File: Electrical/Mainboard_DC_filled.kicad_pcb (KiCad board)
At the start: 2 copper layers, 108 x 88.9 mm, 73 parts, among them J1 Serial Connector, Q1 TIP41C, Q2 TIP41C, U1 L7805CV, U10 6N137, U11 6N137, U12 6N137, U13 6N137, U2 Teensy3.5, U3 L7805CV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

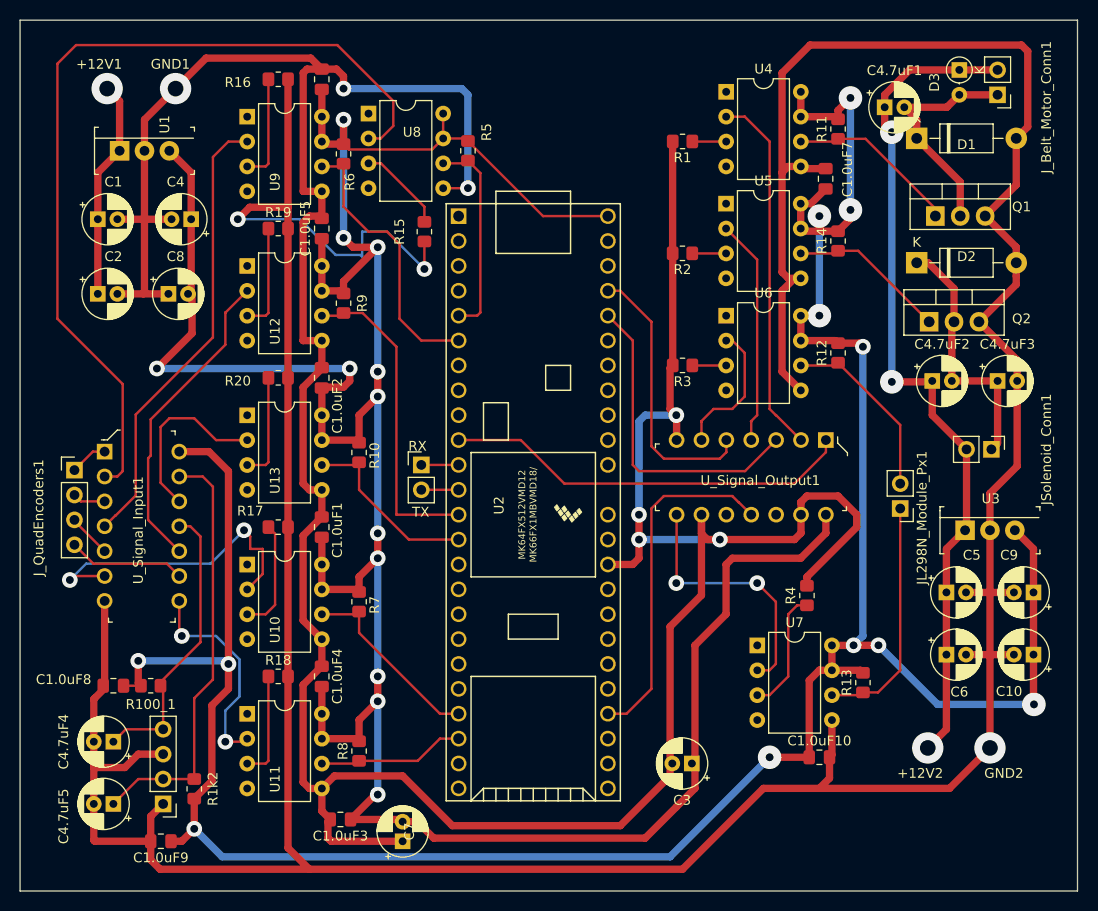
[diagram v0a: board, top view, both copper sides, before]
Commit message: Fixed PCB Error
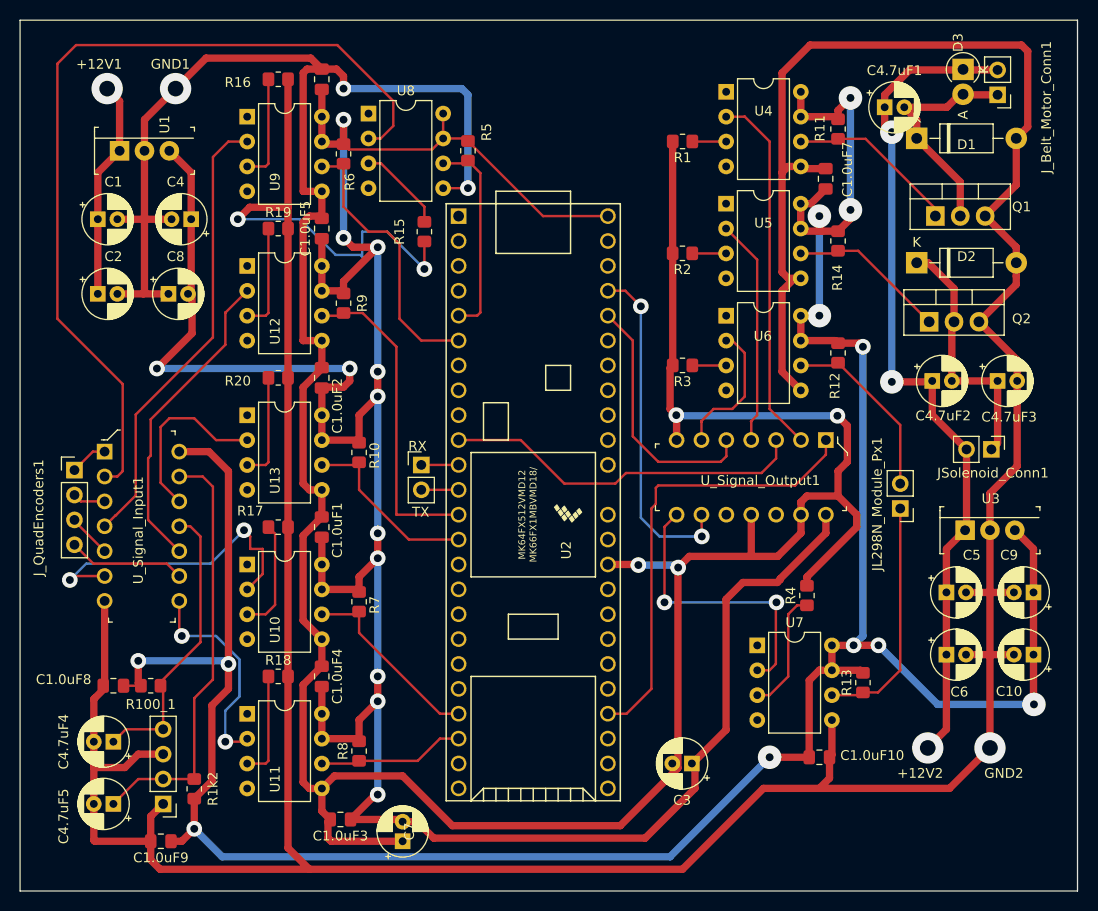
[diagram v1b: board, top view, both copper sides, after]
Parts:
- D3: footprint Diode_THT:D_DO-35_SOD27_P2.54mm_Vertical_AnodeUp -> Diode_THT:D_DO-41_SOD81_P2.54mm_Vertical_AnodeUp
- moved D3 0.39 mm to (196.0, 49.5)
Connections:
- U2 pad 39: unconnected-(U2-Pad39) -> GND1
- U8 pad 2: Net-(U8-Pad2) -> Net-(U8-A)
- U8 pad 3: Net-(R15-Pad1) -> Net-(U8-C)
- U8 pad 6: /QuadDecode1A_Px -> /pg2/QuadDecode1A_Px
- U_Signal_Output1 pad 1: /Print_Solenoid -> /Belt_Motor
- U_Signal_Output1 pad 11: /Belt_Motor -> GND1
- U_Signal_Output1 pad 3: /Px_Motor_Left -> /Print_Solenoid
- U_Signal_Output1 pad 5: /Px_Motor_Right -> /Px_Motor_Left
- U_Signal_Output1 pad 9: GND1 -> /Px_Motor_Right
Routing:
- net /Belt_Motor: track 35.4 -> 46.5 mm
- net /Px_Motor_Right: track 28.2 -> 35.1 mm, vias 0 -> 2
- net /Px_Motor_Left: track 32.5 -> 25.9 mm
- net /Print_Solenoid: track 41.9 -> 37.2 mm
- net Net-(U7-A): track 26.4 -> 29.4 mm
- net GND1: track 339.8 -> 342.2 mm
- net +5VA: track 299.8 -> 297.8 mm
